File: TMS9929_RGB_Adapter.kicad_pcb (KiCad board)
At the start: 2 copper layers, 99.1 x 66 mm, 73 parts, among them P1 CONN_01X06, P10 12V, P2 CONN_01X08, P3 SEL, P4 SEL, P5 SEL, P6 CONN_01X01, P7 CONN_01X01, P8 CONN_01X01, P9 CONN_01X01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

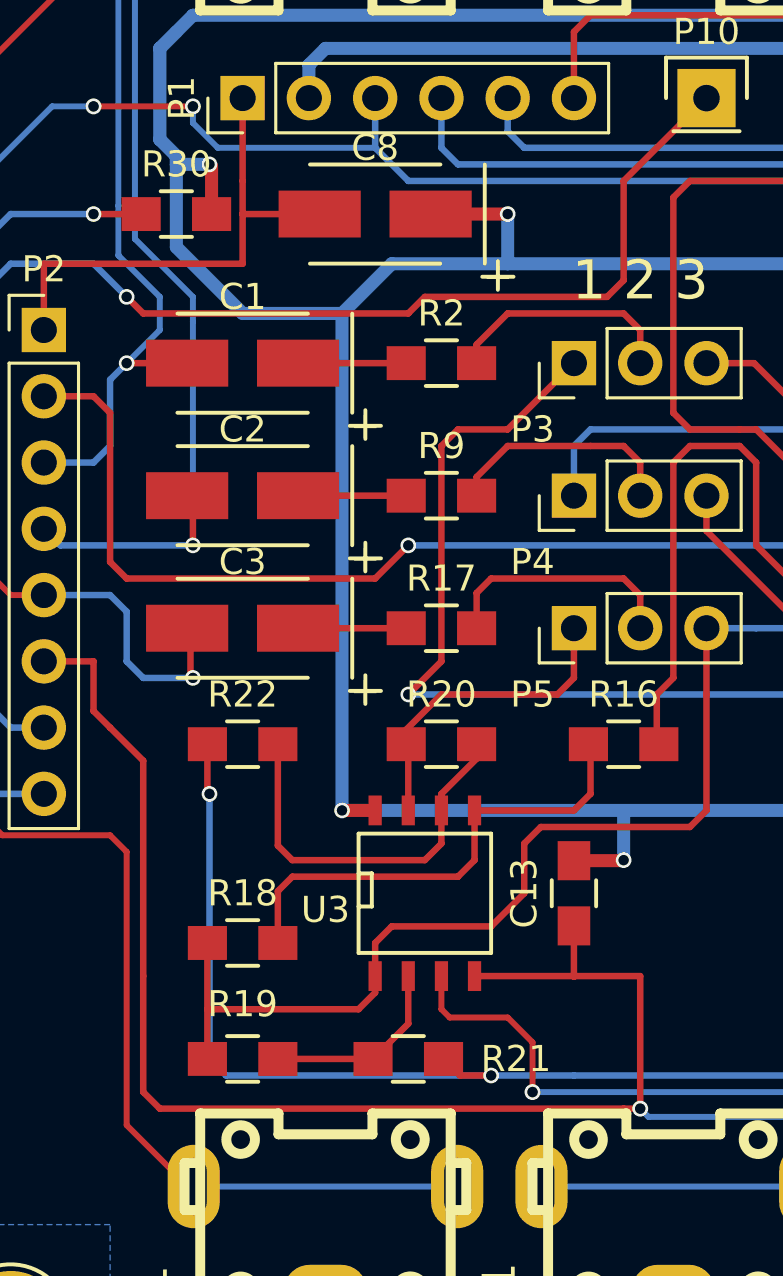
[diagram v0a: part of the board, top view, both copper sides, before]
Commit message: Smaller PCB cosmetics
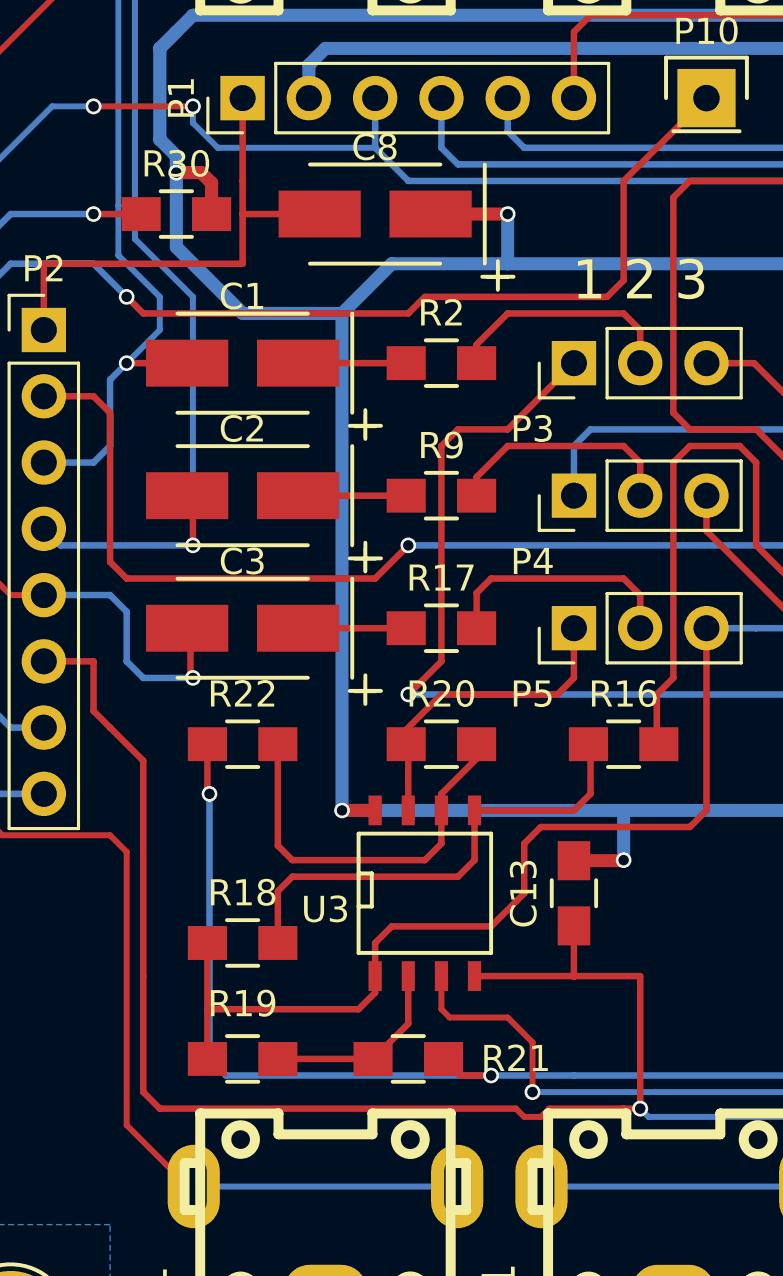
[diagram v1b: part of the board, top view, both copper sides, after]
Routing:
- net VCC: track 248.6 -> 248.1 mm
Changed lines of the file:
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@@
     (thickness 1.6)
     (drawings 10)
-    (tracks 721)
+    (tracks 726)
     (zones 0)
     (modules 73)
@@
   )
   (setup
-    (last_trace_width 0.2286)
+    (last_trace_width 0.508)
     (user_trace_width 0.508)
     (trace_clearance 0.2032)
@@
   (via (at 59.563 114.173) (size 0.6) (drill 0.4) (layers F.Cu B.Cu) (net 3))
   (segment (start 63.46698 112.268) (end 67.738 112.268) (width 0.25) (layer F.Cu) (net 4))
+  (segment (start 73.2155 135.763) (end 72.898 136.0805) (width 0.2286) (layer F.Cu) (net 5))
+  (segment (start 72.263 136.0805) (end 71.9455 135.763) (width 0.2286) (layer F.Cu) (net 5))
+  (segment (start 72.898 136.0805) (end 72.263 136.0805) (width 0.2286) (layer F.Cu) (net 5))
   (segment (start 103.933 100.203) (end 102.743 100.203) (width 0.2286) (layer F.Cu) (net 5))
   (segment (start 102.743 100.203) (end 100.838 102.108) (width 0.2286) (layer F.Cu) (net 5))
@@
   (segment (start 112.983 117.983) (end 113.538 117.983) (width 0.25) (layer F.Cu) (net 5) (status 10))
   (segment (start 53.848 118.618) (end 55.753 118.618) (width 0.25) (layer F.Cu) (net 5))
+  (segment (start 55.753 118.618) (end 55.753 120.523) (width 0.25) (layer F.Cu) (net 5))
+  (segment (start 55.753 120.523) (end 56.388 121.158) (width 0.25) (layer F.Cu) (net 5))
+  (segment (start 57.658 130.683) (end 57.658 135.128) (width 0.25) (layer F.Cu) (net 5))
+  (segment (start 56.388 121.158) (end 57.658 122.428) (width 0.25) (layer F.Cu) (net 5))
+  (segment (start 57.658 122.428) (end 57.658 130.683) (width 0.25) (layer F.Cu) (net 5))
+  (segment (start 58.293 135.763) (end 71.9455 135.763) (width 0.25) (layer F.Cu) (net 5))
   (segment (start 57.658 135.128) (end 58.293 135.763) (width 0.25) (layer F.Cu) (net 5))
-  (segment (start 58.293 135.763) (end 76.073 135.763) (width 0.25) (layer F.Cu) (net 5))
+  (segment (start 73.2155 135.763) (end 76.073 135.763) (width 0.25) (layer F.Cu) (net 5))
   (segment (start 76.073 135.763) (end 76.708 135.763) (width 0.25) (layer F.Cu) (net 5))
-  (segment (start 57.658 122.428) (end 57.658 130.683) (width 0.25) (layer F.Cu) (net 5))
-  (segment (start 56.388 121.158) (end 57.658 122.428) (width 0.25) (layer F.Cu) (net 5))
-  (segment (start 57.658 130.683) (end 57.658 135.128) (width 0.25) (layer F.Cu) (net 5))
-  (segment (start 55.753 120.523) (end 56.388 121.158) (width 0.25) (layer F.Cu) (net 5))
-  (segment (start 55.753 118.618) (end 55.753 120.523) (width 0.25) (layer F.Cu) (net 5))
   (segment (start 53.848 105.918) (end 53.848 103.378) (width 0.25) (layer F.Cu) (net 5))
   (segment (start 61.468 100.203) (end 61.468 101.473) (width 0.25) (layer F.Cu) (net 5))
@@
   (segment (start 108.458 100.203) (end 106.633 100.203) (width 0.25) (layer F.Cu) (net 7) (status 20))
   (segment (start 110.363 100.223) (end 110.383 100.203) (width 0.25) (layer F.Cu) (net 7) (status 30))
+  (segment (start 60.278 101.473) (end 60.278 100.283) (width 0.508) (layer F.Cu) (net 8))
+  (via (at 58.928 99.8855) (size 0.6096) (drill 0.4064) (layers F.Cu B.Cu) (net 8))
+  (segment (start 59.8805 99.8855) (end 58.928 99.8855) (width 0.508) (layer F.Cu) (net 8))
+  (segment (start 60.278 100.283) (end 59.8805 99.8855) (width 0.508) (layer F.Cu) (net 8))
   (segment (start 58.928 99.568) (end 58.928 99.2505) (width 0.508) (layer B.Cu) (net 8))
   (segment (start 58.293 95.123) (end 58.928 94.488) (width 0.508) (layer B.Cu) (net 8))
@@
   (segment (start 59.563 93.853) (end 58.928 94.488) (width 0.5) (layer B.Cu) (net 8))
   (segment (start 94.488 93.853) (end 59.563 93.853) (width 0.5) (layer B.Cu) (net 8))
-  (segment (start 60.198 99.568) (end 58.928 99.568) (width 0.5) (layer B.Cu) (net 8))
   (segment (start 105.918 103.378) (end 103.378 103.378) (width 0.5) (layer F.Cu) (net 8))
   (segment (start 103.378 103.378) (end 103.378 105.303) (width 0.5) (layer F.Cu) (net 8))
-  (segment (start 60.278 99.648) (end 60.278 101.473) (width 0.5) (layer F.Cu) (net 8))
-  (segment (start 60.198 99.568) (end 60.278 99.648) (width 0.5) (layer F.Cu) (net 8))
   (segment (start 106.426 122.428) (end 106.553 122.555) (width 0.25) (layer F.Cu) (net 8))
   (segment (start 102.743 124.333) (end 102.743 124.353) (width 0.25) (layer F.Cu) (net 8))
   (segment (start 103.378 105.303) (end 103.378 104.648) (width 0.25) (layer F.Cu) (net 8))
   (segment (start 61.468 105.283) (end 65.278 105.283) (width 0.5) (layer B.Cu) (net 8))
-  (segment (start 58.928 99.568) (end 58.928 102.743) (width 0.5) (layer B.Cu) (net 8))
+  (segment (start 58.928 99.568) (end 58.928 99.8855) (width 0.5) (layer B.Cu) (net 8))
+  (segment (start 58.928 99.8855) (end 58.928 102.743) (width 0.5) (layer B.Cu) (net 8))
   (segment (start 90.043 103.378) (end 92.583 103.378) (width 0.5) (layer F.Cu) (net 8))
   (segment (start 90.043 105.303) (end 90.043 103.378) (width 0.5) (layer F.Cu) (net 8))
@@
   (segment (start 88.793 124.353) (end 88.773 124.333) (width 0.5) (layer F.Cu) (net 8))
   (segment (start 90.043 105.303) (end 90.043 105.283) (width 0.25) (layer F.Cu) (net 8))
-  (via (at 60.198 99.568) (size 0.6) (drill 0.4) (layers F.Cu B.Cu) (net 8))
   (segment (start 92.028 113.538) (end 92.028 112.188) (width 0.25) (layer F.Cu) (net 9) (status 10))
   (segment (start 97.028 103.378) (end 98.298 104.648) (width 0.25) (layer F.Cu) (net 9))

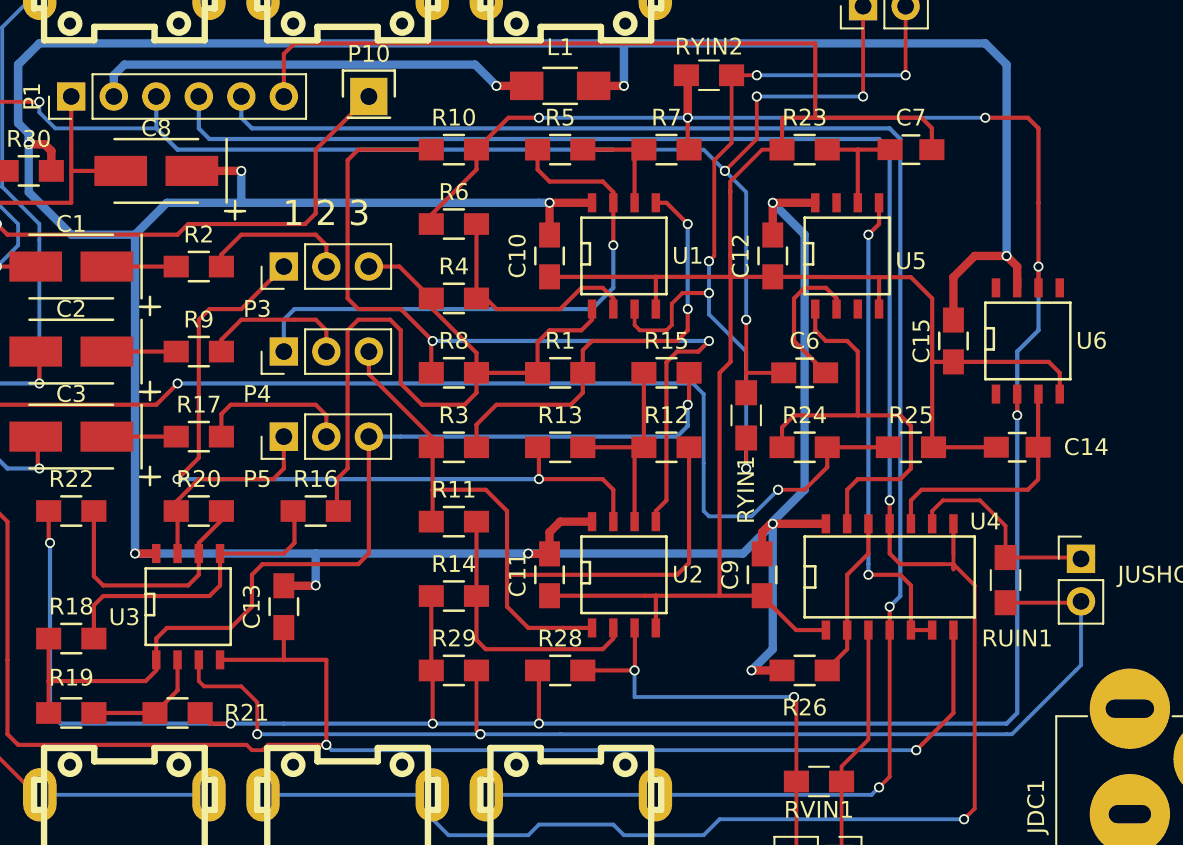
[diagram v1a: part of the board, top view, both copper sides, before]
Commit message: Added new resistors in parallel to existing ones to solder standard resistor values
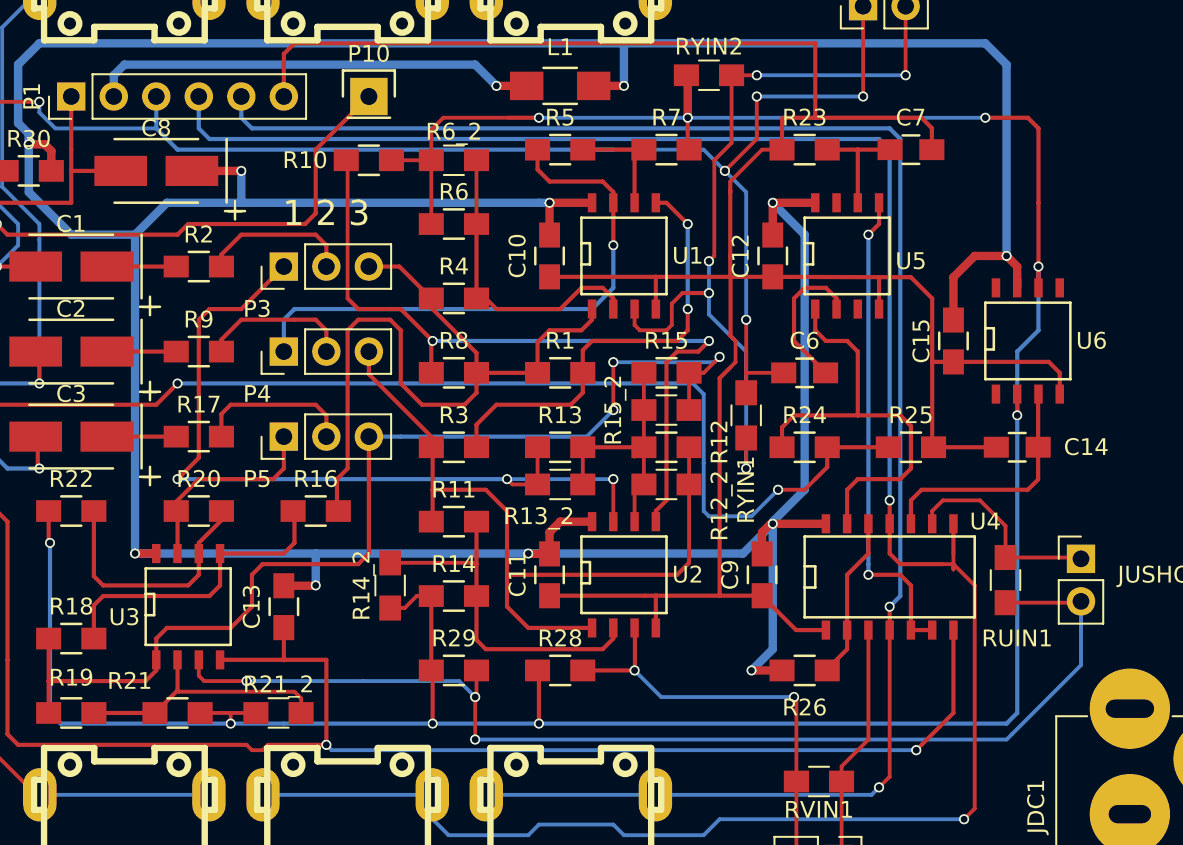
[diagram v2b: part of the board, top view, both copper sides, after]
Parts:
- added R12_2: 68k, Resistors_SMD:R_0805_HandSoldering, F.Cu at (97.0, 120.2)
- added R13_2: 10k, Resistors_SMD:R_0805_HandSoldering, F.Cu at (90.7, 120.2)
- added R14_2: 12k, Resistors_SMD:R_0805_HandSoldering, F.Cu at (80.5, 126.2)
- added R15_2: 100k, Resistors_SMD:R_0805_HandSoldering, F.Cu at (97.0, 115.8)
- added R21_2: 12k, Resistors_SMD:R_0805_HandSoldering, F.Cu at (73.9, 133.9)
- added R6_2: 12k, Resistors_SMD:R_0805_HandSoldering, F.Cu at (84.3, 100.8)
- R12: value 6.2k -> 6.8k
- R13: value 3.6k -> 5.6k
- R14, R21, R6: value 2k -> 2k7
- R15: value 9.1k -> 10k
- RUIN1, RVIN1, RYIN1: value 10E -> 4.7k
- moved R10 5.12 mm to (79.2, 100.8)
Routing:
- net /Vref: track 166.7 -> 176.7 mm
- net Net-(R19-Pad2): track 7.38 -> 15.8 mm
- net /B-Y: track 58.6 -> 65.1 mm, vias 1 -> 3
- net Net-(R11-Pad2): track 16.4 -> 21.7 mm
- net Net-(R10-Pad1): track 51.1 -> 45.8 mm
- net Net-(R4-Pad2): track 14.3 -> 18.1 mm
- net Net-(R12-Pad1): track 13.0 -> 16.0 mm
- net /G: track 46.7 -> 49.4 mm, vias 2 -> 3
- net Net-(JUSHORT1-Pad2): track 70.5 -> 68.7 mm, vias 2 -> 3
- net Net-(JVSHORT1-Pad2): track 26.5 -> 25.6 mm
